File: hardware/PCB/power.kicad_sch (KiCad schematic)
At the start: 0 parts

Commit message: Schematic - Added Buck ICs
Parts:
- added C1, C10, C12, C13, C2, C4, C5, C6, C8, C9: ?, symbol Device:C
- added C11: 0.1u, symbol Device:C
- added C3, C7: 100n, symbol Device:C
- added L1, L2, L3: L, symbol Device:L
- added R1, R2, R3, R4, R5, R6, R7, R8, R9: ?, symbol Device:R_US
- added U1, U3: TPS62933, Package_TO_SOT_SMD:SOT-583-8, symbol Regulator_Switching:TPS62933
- added U2: TPS568215RNN, Package_DFN_QFN:Texas_RNN0018A, symbol Regulator_Switching:TPS568215RNN
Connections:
- new net: C11.2, U2.1 (BOOT)
- new net: R8.2, R9.1, U2.13 (FB)
- new net: C13.1, U2.14 (SS)
- new net: R7.1, U2.18 (MODE)
- new net: C11.1, L3.1, U2.6 (SW), U2.7 (SW)
- new net: R5.2, R6.1, U3.8 (FB)
- new net: R4.2, U3.1 (RT)
- new net: C2.2, U1.7 (SS)
- new net: C7.2, L2.1, U3.5 (SW)
- new net: C7.1, U3.6 (BST)
- new net: C6.2, U3.7 (SS)
- new net: C3.2, L1.1, U1.5 (SW)
- new net: R1.2, U1.1 (RT)
- new net: C3.1, U1.6 (BST)
- new net: R2.2, R3.1, U1.8 (FB)
- new net +24V: C1.2, C10.2, C5.2, C9.2, U1.2 (EN), U1.3 (VIN), U2.11 (VIN), U2.2 (VIN), U3.2 (EN), U3.3 (VIN)
- new net 3.3 V: C4.1, L1.2, R2.1
- new net 5 V: C8.1, L2.2, R5.1
- new net 5-15 V: C12.1, L3.2, R8.1
- new net GND: C1.1, C10.1, C12.2, C13.2, C2.1, C4.2, C5.1, C6.1, C8.2, C9.1, R1.1, R3.2, R4.1, R6.2, R7.2, R9.2, U1.4 (GND), U2.10 (PGND), U2.12 (AGND), U2.3 (PGND), U2.4 (PGND), U2.5 (PGND), U2.8 (PGND), U2.9 (PGND), U3.4 (GND)
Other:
- note added: "Topiary Trimbot - Power"

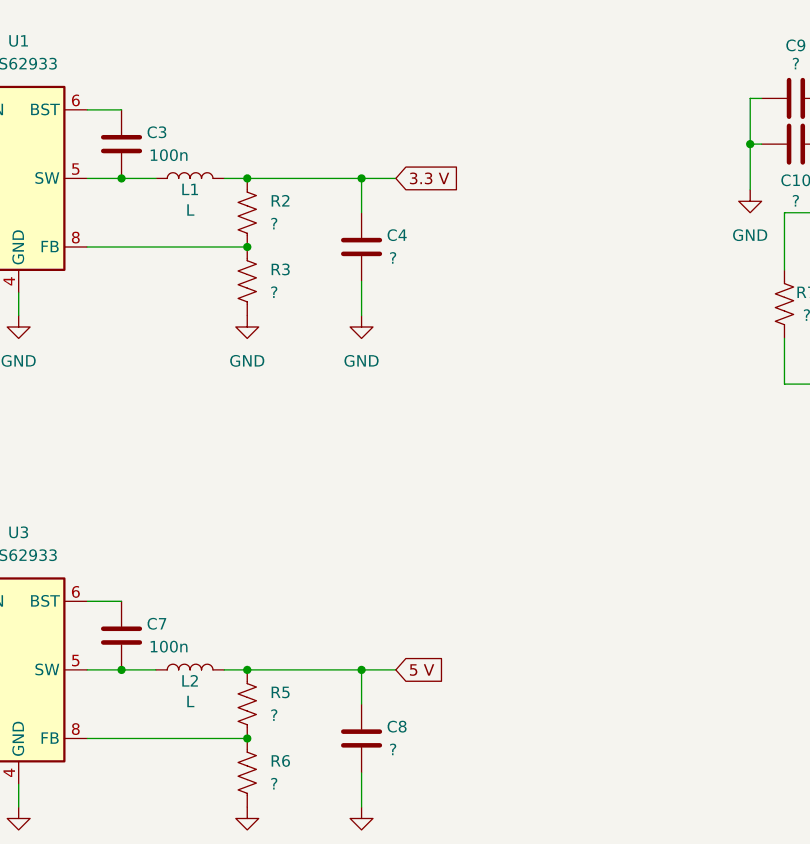
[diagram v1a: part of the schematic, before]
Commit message: Schematic - Power Flags
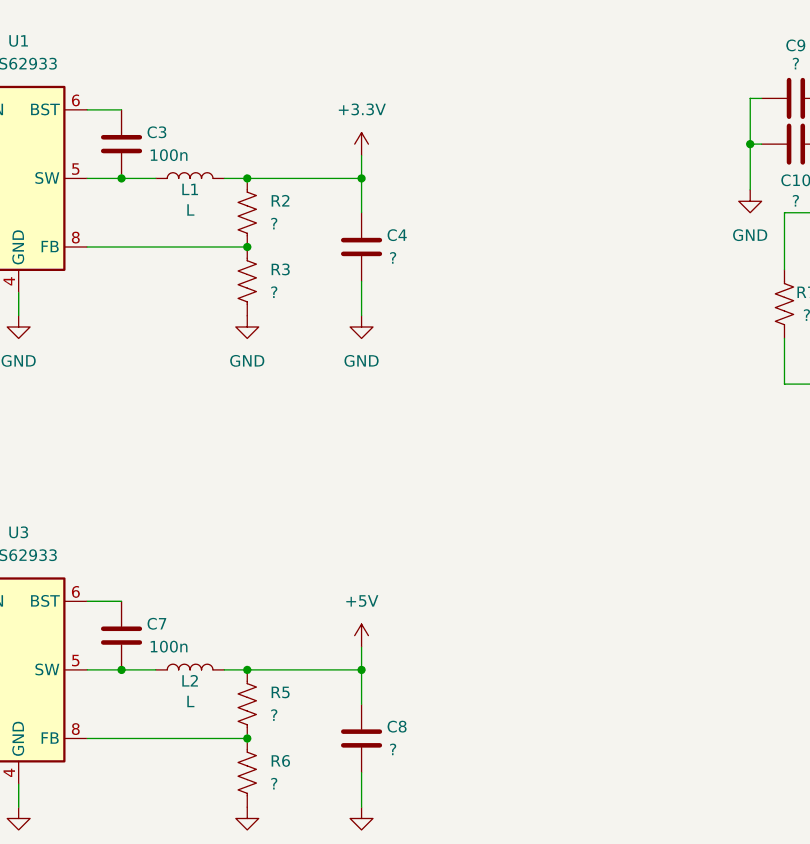
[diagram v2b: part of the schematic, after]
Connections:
- net 3.3 V renamed +3.3V
- net 5 V renamed +5V
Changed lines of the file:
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@@
 	)
 	(junction
+		(at 101.6 52.07)
+		(diameter 0)
+		(color 0 0 0 0)
+	)
+	(junction
 		(at 50.8 101.6)
 		(diameter 0)
@@
 	)
 	(junction
-		(at 101.6 52.07)
+		(at 101.6 106.68)
 		(diameter 0)
 		(color 0 0 0 0)
@@
 	)
 	(junction
-		(at 101.6 106.68)
-		(diameter 0)
-		(color 0 0 0 0)
-	)
-	(junction
 		(at 207.01 45.72)
 		(diameter 0)
@@
 	(wire
 		(pts
-			(xy 101.6 52.07) (xy 105.41 52.07)
-		)
-		(stroke
-			(width 0)
-			(type default)
-		)
-	)
-	(wire
-		(pts
 			(xy 74.93 106.68) (xy 78.74 106.68)
 		)
@@
 	(wire
 		(pts
+			(xy 101.6 104.14) (xy 101.6 106.68)
+		)
+		(stroke
+			(width 0)
+			(type default)
+		)
+	)
+	(wire
+		(pts
 			(xy 74.93 52.07) (xy 78.74 52.07)
 		)
@@
 	(wire
 		(pts
+			(xy 101.6 49.53) (xy 101.6 52.07)
+		)
+		(stroke
+			(width 0)
+			(type default)
+		)
+	)
+	(wire
+		(pts
 			(xy 48.26 46.99) (xy 50.8 46.99)
 		)
@@
 	(wire
 		(pts
-			(xy 101.6 106.68) (xy 105.41 106.68)
-		)
-		(stroke
-			(width 0)
-			(type default)
-		)
-	)
-	(wire
-		(pts
 			(xy 39.37 46.99) (xy 39.37 48.26)
 		)
@@
 		)
 	)
-	(global_label "5 V"
-		(shape input)
-		(at 105.41 106.68 0)
-		(fields_autoplaced yes)
-		(effects
-			(font
-				(size 1.27 1.27)
-			)
-			(justify left)
-		)
-		(property "Intersheetrefs" "${INTERSHEET_REFS}"
-			(at 111.6609 106.68 0)
-			(effects
-				(font
-					(size 1.27 1.27)
-				)
-				(justify left)
-				(hide yes)
-			)
-		)
-	)
 	(global_label "5-15 V"
 		(shape input)
@@
 		)
 	)
-	(global_label "3.3 V"
-		(shape input)
-		(at 105.41 52.07 0)
-		(fields_autoplaced yes)
-		(effects
-			(font
-				(size 1.27 1.27)
-			)
-			(justify left)
-		)
-		(property "Intersheetrefs" "${INTERSHEET_REFS}"
-			(at 113.4752 52.07 0)
-			(effects
-				(font
-					(size 1.27 1.27)
-				)
-				(justify left)
-				(hide yes)
-			)
-		)
-	)
 	(symbol
 		(lib_id "Regulator_Switching:TPS568215RNN")
@@
 	)
 	(symbol
+		(lib_id "power:+3.3V")
+		(at 101.6 49.53 0)
+		(unit 1)
+		(exclude_from_sim no)
+		(in_bom yes)
+		(on_board yes)
+		(dnp no)
+		(fields_autoplaced yes)
+		(property "Reference" "#PWR018"
+			(at 101.6 53.34 0)
+			(effects
+				(font
+					(size 1.27 1.27)
+				)
+				(hide yes)
+			)
+		)
+		(property "Value" "+3.3V"
+			(at 101.6 44.45 0)
+			(effects
+				(font
+					(size 1.27 1.27)
+				)
+			)
+		)
+		(property "Footprint" ""
+			(at 101.6 49.53 0)
+			(effects
+				(font
+					(size 1.27 1.27)
+				)
+				(hide yes)
+			)
+		)
+		(property "Datasheet" ""
+			(at 101.6 49.53 0)
+			(effects
+				(font
+					(size 1.27 1.27)
+				)
+				(hide yes)
+			)
+		)
+		(property "Description" "Power symbol creates a global label with name \"+3.3V\""
+			(at 101.6 49.53 0)
+			(effects
+				(font
+					(size 1.27 1.27)
+				)
+				(hide yes)
+			)
+		)
+		(pin "1"
+		)
+		(instances
+			(project ""
+				(path "/288cd01c-b1d5-44ca-91a2-b9192151afef"
+					(reference "#PWR018")
+					(unit 1)
+				)
+			)
+		)
+	)
+	(symbol
 		(lib_id "Device:C")
 		(at 52.07 109.22 90)
@@
 					(unit 1)
 				)
+			)
+		)
+	)
+	(symbol
+		(lib_id "power:+5V")
+		(at 101.6 104.14 0)
+		(unit 1)
+		(exclude_from_sim no)
+		(in_bom yes)
+		(on_board yes)
+		(dnp no)
+		(fields_autoplaced yes)
+		(property "Reference" "#PWR019"
+			(at 101.6 107.95 0)
+			(effects
+				(font
+					(size 1.27 1.27)
+				)
+				(hide yes)
+			)
+		)
+		(property "Value" "+5V"
+			(at 101.6 99.06 0)
+			(effects
+				(font
+					(size 1.27 1.27)
+				)
+			)
+		)
+		(property "Footprint" ""
+			(at 101.6 104.14 0)
+			(effects
+				(font
+					(size 1.27 1.27)
+				)
+				(hide yes)
+			)
+		)
+		(property "Datasheet" ""
+			(at 101.6 104.14 0)
+			(effects
+				(font
+					(size 1.27 1.27)
+				)
+				(hide yes)
+			)
+		)
+		(property "Description" "Power symbol creates a global label with name \"+5V\""
+			(at 101.6 104.14 0)
+			(effects
+				(font
+					(size 1.27 1.27)
+				)
+				(hide yes)
+			)
+		)
+		(pin "1"
+		)
+		(instances
+			(project ""
+				(path "/288cd01c-b1d5-44ca-91a2-b9192151afef"
+					(reference "#PWR019")
+					(unit 1)
+				)

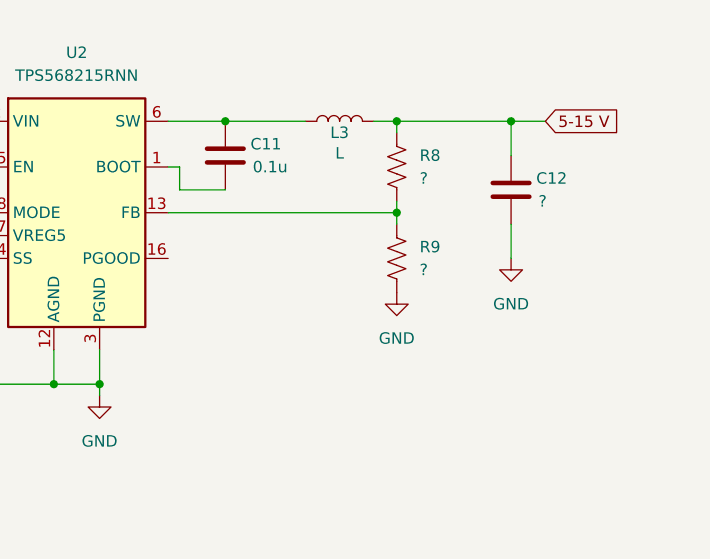
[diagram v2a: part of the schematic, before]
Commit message: Schematic - Power flag
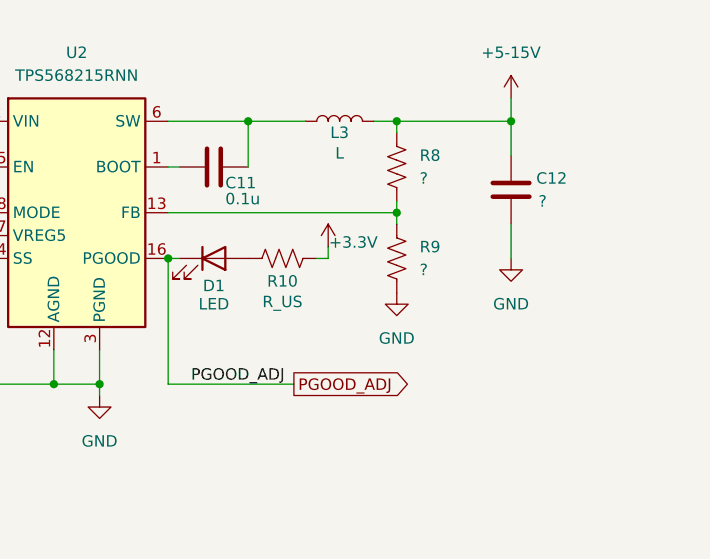
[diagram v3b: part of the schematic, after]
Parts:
- added D1: LED, symbol Device:LED
- added R10: R_US, symbol Device:R_US
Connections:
- net +3.3V: now also R10.1
- net PGOOD_ADJ: now reaches U2.16 (PGOOD)
- net PGOOD_ADJ: now also D1.1 (K)
- net 5-15 V renamed +5-15V
- new net: D1.2 (A), R10.2
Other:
- moved on the sheet: C11

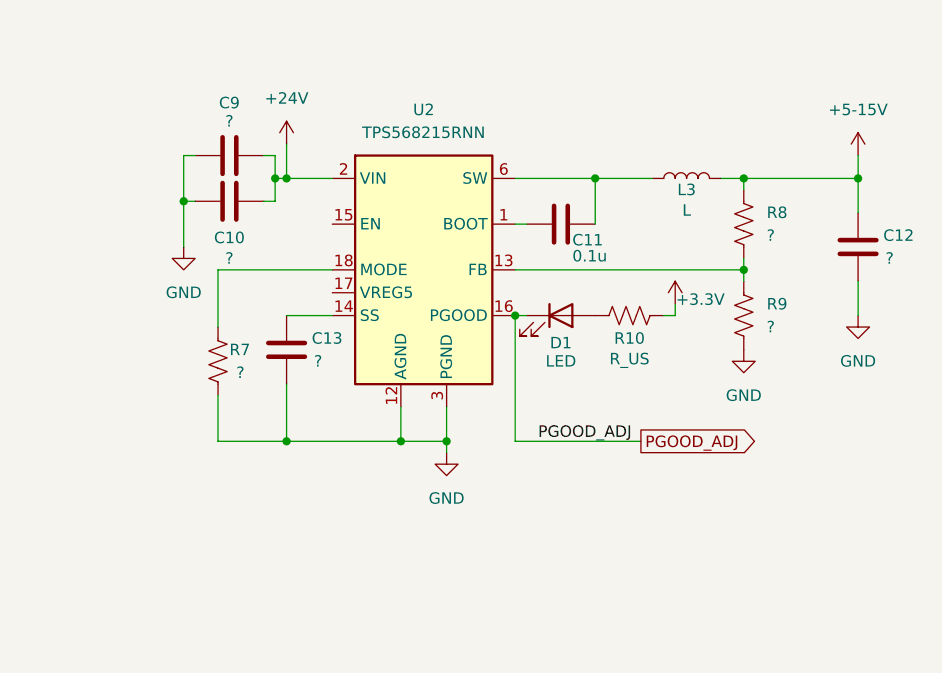
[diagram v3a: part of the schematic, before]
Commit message: Schematic - Placed Correct 5-15 Buck IC
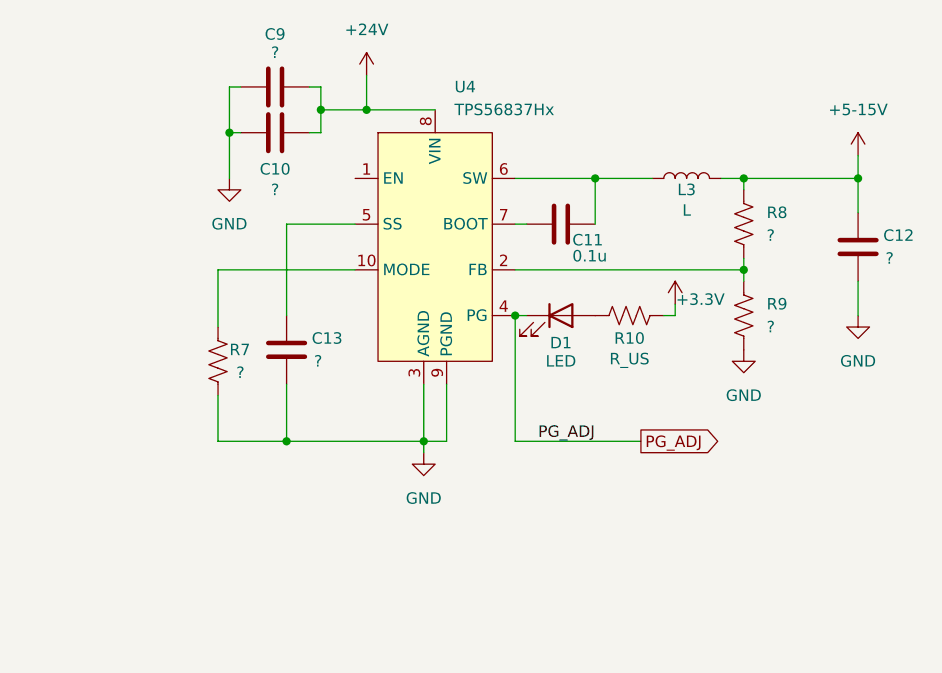
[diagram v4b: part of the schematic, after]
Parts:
- removed U2: TPS568215RNN, Package_DFN_QFN:Texas_RNN0018A, symbol Regulator_Switching:TPS568215RNN
- added U4: TPS56837Hx, CustomFootprints:RPA0010A-MFG, symbol CustomSymbols:TPS56837Hx
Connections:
- net +24V: now also U4.8 (VIN)
- net GND: now also U4.3 (AGND), U4.9 (PGND)
- net at C11.2: now also U4.7 (BOOT)
- net at R8.2, R9.1: now also U4.2 (FB)
- net at C13.1: now also U4.5 (SS)
- net at R7.1: now also U4.10 (MODE)
- net at C11.1, L3.1: now also U4.6 (SW)
- net PGOOD_ADJ renamed PG_ADJ
- net PG_ADJ: now also U4.4 (PG)
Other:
- moved on the sheet: C10, C9

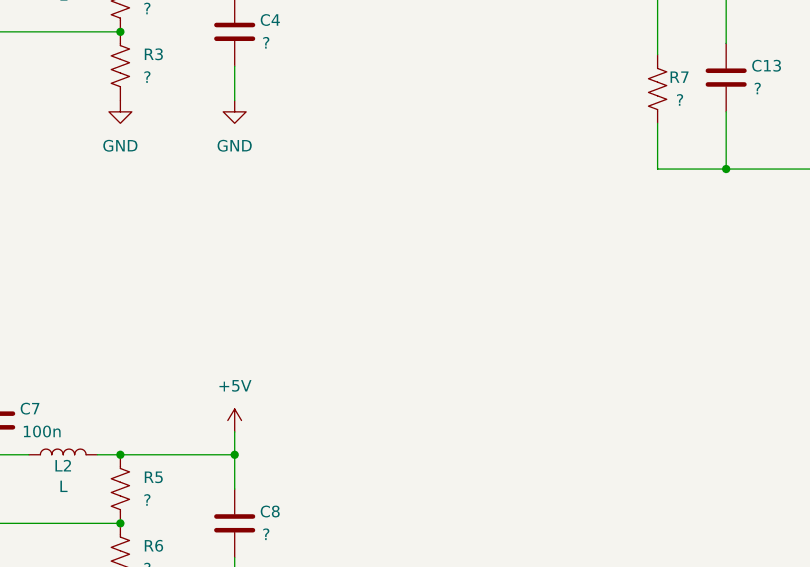
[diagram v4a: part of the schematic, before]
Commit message: Schematic - 24 V Screw Terminal
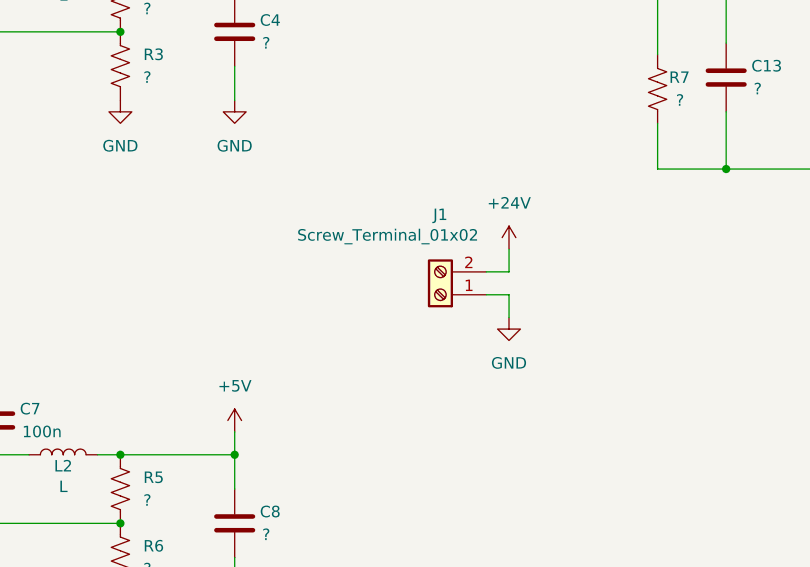
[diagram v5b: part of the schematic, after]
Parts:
- added J1: Screw_Terminal_01x02, symbol Connector:Screw_Terminal_01x02
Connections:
- net +24V: now also J1.2 (Pin_2)
- net GND: now also J1.1 (Pin_1)

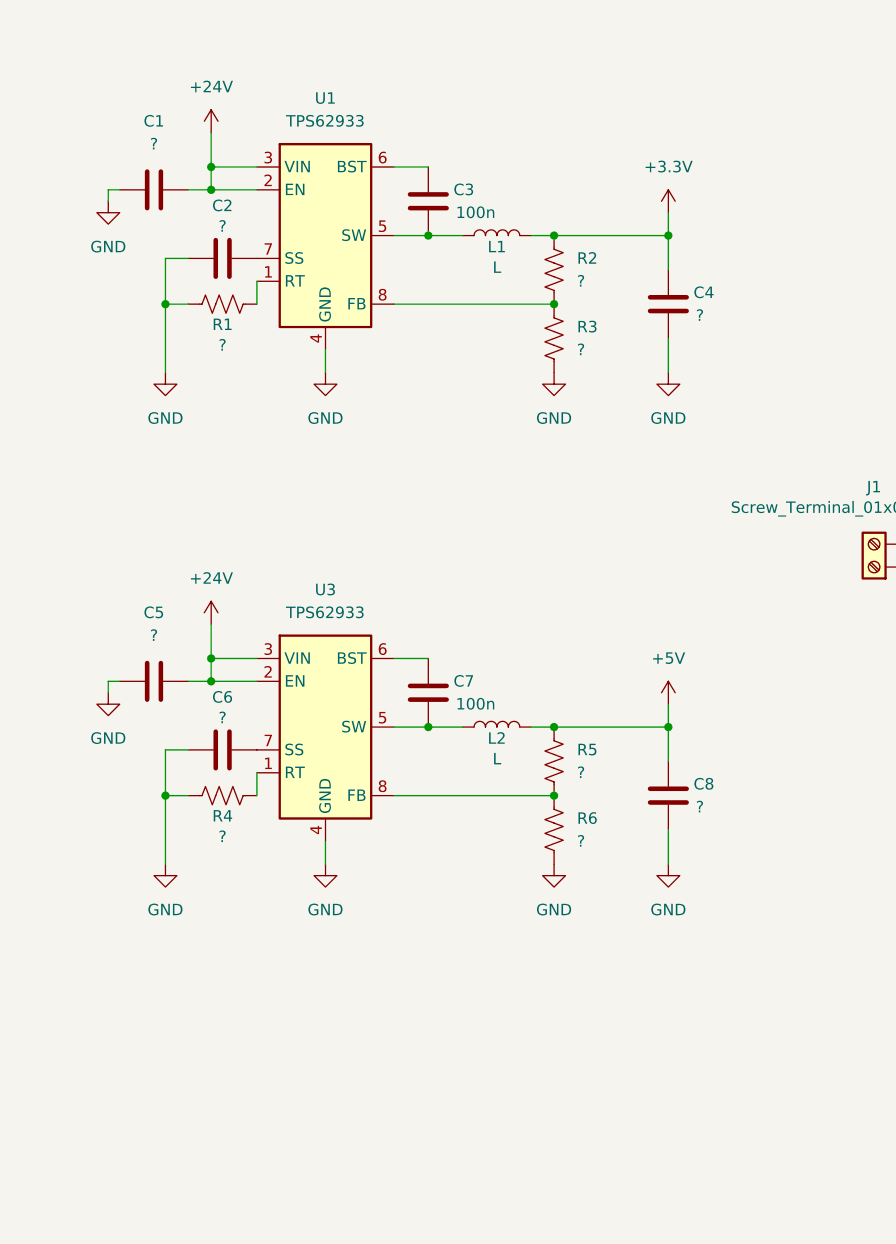
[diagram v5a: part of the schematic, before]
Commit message: Schematic - Buck Converter Passives
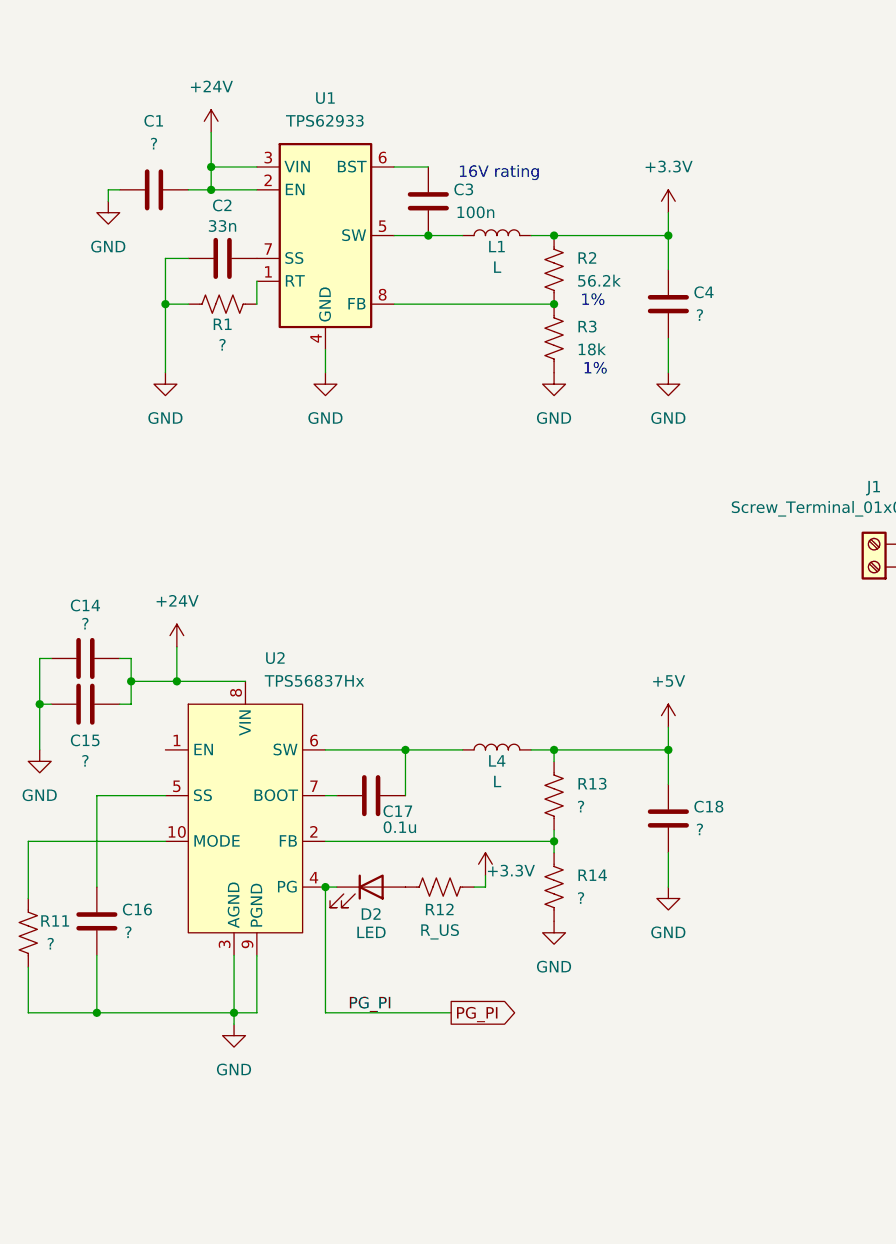
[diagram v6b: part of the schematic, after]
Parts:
- removed C5, C6, C8: ?, symbol Device:C
- removed C7: 100n, symbol Device:C
- removed L2: L, symbol Device:L
- removed R4, R5, R6: ?, symbol Device:R_US
- removed U3: TPS62933, Package_TO_SOT_SMD:SOT-583-8, symbol Regulator_Switching:TPS62933
- added C14, C15, C16, C18: ?, symbol Device:C
- added C17: 0.1u, symbol Device:C
- added D2: LED, symbol Device:LED
- added L4: L, symbol Device:L
- added R11, R13, R14: ?, symbol Device:R_US
- added R12: R_US, symbol Device:R_US
- added U2: TPS56837Hx, CustomFootprints:RPA0010A-MFG, symbol CustomSymbols:TPS56837Hx
- C2: value ? -> 33n
- R2: value ? -> 56.2k
- R3: value ? -> 18k
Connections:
- net +24V: now also C14.2, C15.2, U2.8 (VIN)
- net +3.3V: now also R12.1
- net +5V: now also C18.1, L4.2, R13.1
- net GND: now also C14.1, C15.1, C16.2, C18.2, R11.2, R14.2, U2.3 (AGND), U2.9 (PGND)
- new net: C16.1, U2.5 (SS)
- new net: D2.2 (A), R12.2
- new net: R11.1, U2.10 (MODE)
- new net: R13.2, R14.1, U2.2 (FB)
- new net: C17.1, L4.1, U2.6 (SW)
- new net: C17.2, U2.7 (BOOT)
- new net PG_PI: D2.1 (K), U2.4 (PG)
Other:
- note added: "1%"
- note added: "16V rating"
